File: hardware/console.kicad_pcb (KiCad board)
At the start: 2 copper layers, 44 x 72 mm, 51 parts, among them J1 USB-C_Module, J3 SWD, J4 UART, J5 LiPo_140mAh, SW1 SW_LEFT, SW2 SW_RIGHT, SW3 SW_UP, SW4 SW_DOWN, SW5 SW_A, SW6 SW_B, SW7 SW_POWER, SW8 SW_START, SW9 SW_SELECT, U1 STM32G0B1CBT6, U2 XC6206P332MR, U3 TP4054

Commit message: change the mcu ... again
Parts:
- U1: value STM32G0B1CBT6 -> STM32G070CBT6
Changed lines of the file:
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@@
 			)
 		)
-		(property "Value" "STM32G0B1CBT6"
+		(property "Value" "STM32G070CBT6"
 			(at 0 5.85 0)
 			(layer "F.Fab")
@@
 			)
 		)
-		(property "Datasheet" "https://www.st.com/resource/en/datasheet/stm32g0b1cb.pdf"
+		(property "Datasheet" "https://www.st.com/resource/en/datasheet/stm32g070cb.pdf"
 			(at 0 0 0)
 			(layer "F.Fab")
@@
 			)
 		)
-		(property "Description" "STMicroelectronics Arm Cortex-M0+ MCU, 128KB flash, 144KB RAM, 64 MHz, 1.7-3.6V, USB 2.0 FS, 44 GPIO, LQFP48"
+		(property "Description" "STMicroelectronics Arm Cortex-M0+ MCU, 128KB flash, 36KB RAM, 64 MHz, 2.0-3.6V, 43 GPIO, LQFP48"
 			(at 0 0 0)
 			(layer "F.Fab")
@@
 			)
 		)
-		(property "LCSC" "C2847904"
+		(property "LCSC" "C529338"
 			(at 0 0 0)
 			(unlocked yes)
@@
 			)
 		)
-		(property "MPN" "STM32G0B1CBT6"
+		(property "MPN" "STM32G070CBT6"
 			(at 0 0 0)
 			(unlocked yes)
@@
 			(unit
 				(name "A")
-				(pins "5" "8" "9" "10" "38" "39" "40" "41" "30" "31" "1" "2" "3" "4"
-					"7" "6" "11" "12" "13" "14" "15" "16" "17" "18" "28" "33" "29" "34"
-					"32" "35" "36" "37" "19" "20" "21" "42" "43" "44" "45" "46" "47" "48"
-					"22" "23" "24" "25" "26" "27"
+				(pins "10" "5" "8" "9" "38" "39" "40" "41" "30" "31" "1" "2" "3" "32"
+					"29" "4" "7" "6" "11" "12" "13" "14" "15" "16" "17" "18" "28" "33" "34"
+					"35" "36" "37" "19" "20" "21" "42" "43" "44" "45" "46" "47" "48" "22"
+					"23" "24" "25" "26" "27"
 				)
 			)
@@
 			(roundrect_rratio 0.25)
 			(net "/NRST")
-			(pinfunction "PF2_10")
-			(pintype "bidirectional")
+			(pinfunction "NRST_10")
+			(pintype "input")
 		)
 		(pad "11" smd roundrect
@@
 			(layers "F.Cu" "F.Mask" "F.Paste")
 			(roundrect_rratio 0.25)
-			(net "unconnected-(U1-PA9{slash}UCPD1_DBCC1-Pad29)")
-			(pinfunction "PA9/UCPD1_DBCC1_29")
-			(pintype "bidirectional+no_connect")
+			(net "unconnected-(U1-NC{slash}PA9-Pad29)")
+			(pinfunction "NC/PA9_29")
+			(pintype "no_connect")
 		)
 		(pad "30" smd roundrect
@@
 			(layers "F.Cu" "F.Mask" "F.Paste")
 			(roundrect_rratio 0.25)
-			(net "unconnected-(U1-PA10{slash}UCPD1_DBCC2-Pad32)")
-			(pinfunction "PA10/UCPD1_DBCC2_32")
-			(pintype "bidirectional+no_connect")
+			(net "unconnected-(U1-NC{slash}PA10-Pad32)")
+			(pinfunction "NC/PA10_32")
+			(pintype "no_connect")
 		)
 		(pad "33" smd roundrect

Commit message: pushbutton values
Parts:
- SW1: value SW_LEFT -> SW_PUSH
- SW2: value SW_RIGHT -> SW_PUSH
- SW3: value SW_UP -> SW_PUSH
- SW4: value SW_DOWN -> SW_PUSH
- SW5: value SW_A -> SW_PUSH
- SW6: value SW_B -> SW_PUSH
- SW8: value SW_START -> SW_PUSH
- SW9: value SW_SELECT -> SW_PUSH
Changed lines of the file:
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@@
 			)
 		)
-		(property "Value" "SW_RIGHT"
+		(property "Value" "SW_PUSH"
 			(at 0 2.65 90)
 			(layer "F.Fab")
@@
 			)
 		)
-		(property "Value" "SW_START"
+		(property "Value" "SW_PUSH"
 			(at 0.000001 2.65 335)
 			(layer "F.Fab")
@@
 			)
 		)
-		(property "Value" "SW_UP"
+		(property "Value" "SW_PUSH"
 			(at 0 2.65 0)
 			(layer "F.Fab")
@@
 			)
 		)
-		(property "Value" "SW_A"
+		(property "Value" "SW_PUSH"
 			(at 0 2.65 0)
 			(layer "F.Fab")
@@
 			)
 		)
-		(property "Value" "SW_DOWN"
+		(property "Value" "SW_PUSH"
 			(at 0 2.65 0)
 			(layer "F.Fab")
@@
 			)
 		)
-		(property "Value" "SW_B"
+		(property "Value" "SW_PUSH"
 			(at 0 2.65 0)
 			(layer "F.Fab")
@@
 			)
 		)
-		(property "Value" "SW_SELECT"
+		(property "Value" "SW_PUSH"
 			(at 0.000001 2.65 335)
 			(layer "F.Fab")
@@
 			)
 		)
-		(property "Value" "SW_LEFT"
+		(property "Value" "SW_PUSH"
 			(at 0 2.65 90)
 			(layer "F.Fab")

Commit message: delete more stuff
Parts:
- removed TP3: +3.3V, TestPoint:TestPoint_THTPad_D1.5mm_Drill0.7mm
- removed TP4: VBUS, TestPoint:TestPoint_THTPad_D1.5mm_Drill0.7mm
- removed TP8: I2C_SDA, TestPoint:TestPoint_THTPad_D1.5mm_Drill0.7mm
- removed TP9: I2C_SCL, TestPoint:TestPoint_THTPad_D1.5mm_Drill0.7mm
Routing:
- net /I2C_SDA: track 46.2 -> 44.1 mm
- net VBUS: vias 0 -> 1
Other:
- board text removed: "3V3"
- board text removed: "SCL"
- board text removed: "SDA"
- board text removed: "VB"

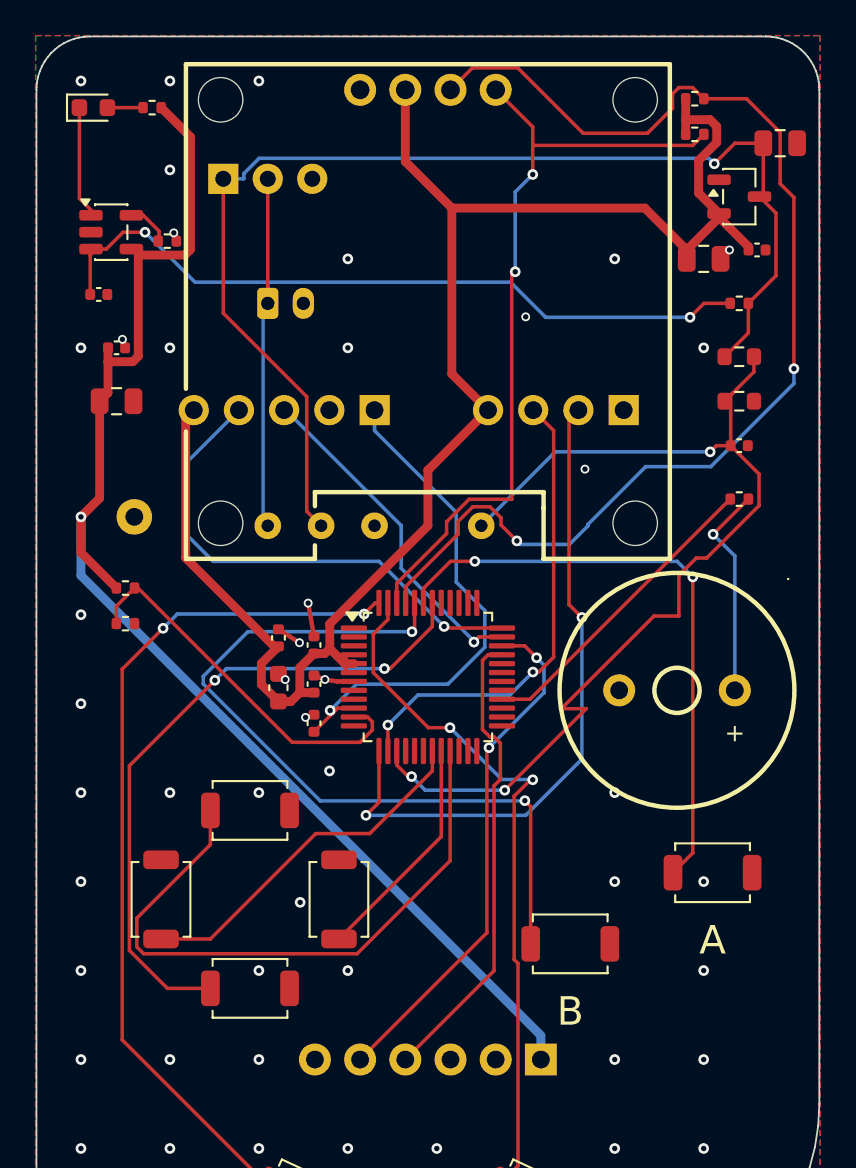
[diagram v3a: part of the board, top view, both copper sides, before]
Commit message: move switch and chrg led to the top right
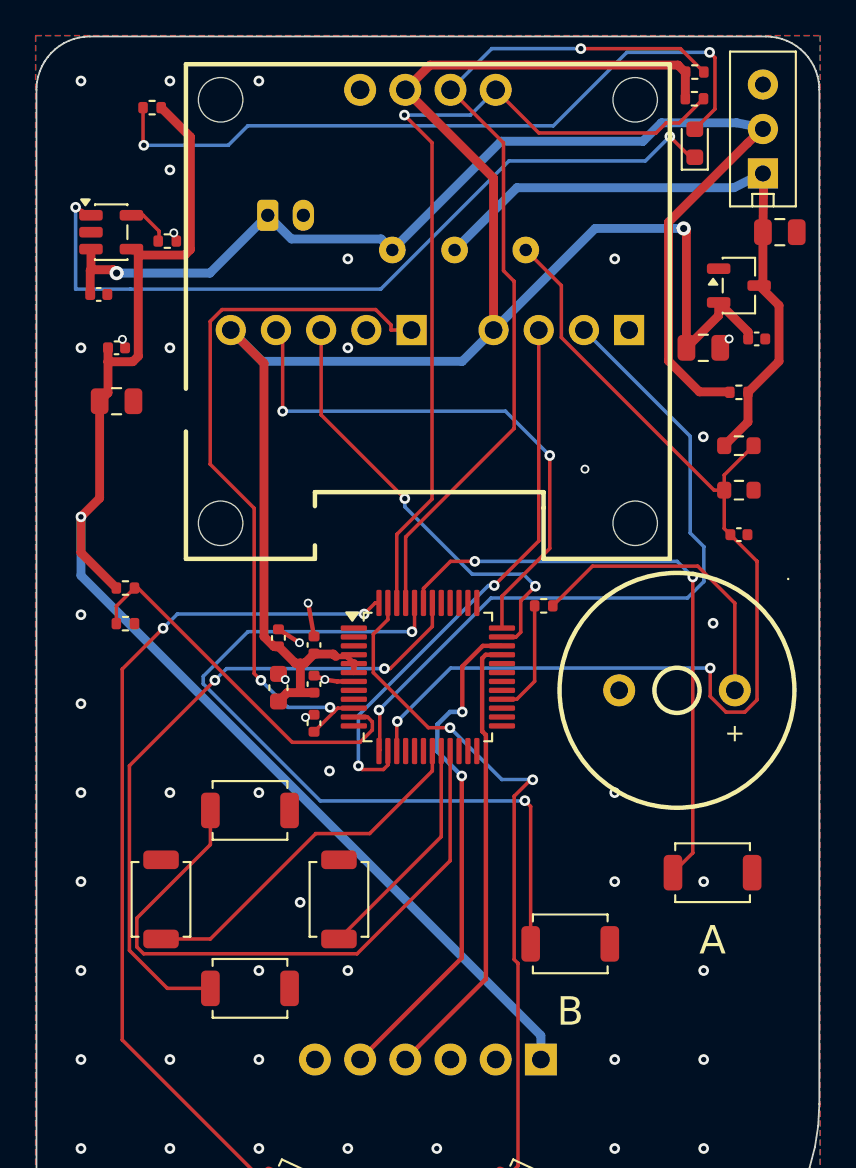
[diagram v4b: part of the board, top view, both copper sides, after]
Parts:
- removed TP1: GND, TestPoint:TestPoint_Loop_D2.50mm_Drill1.0mm
- removed TP2: GND, TestPoint:TestPoint_THTPad_D1.5mm_Drill0.7mm
- SW7: moved to F.Cu
- moved D1 33.9 mm to (37.0, 6.00), turned to 90 degrees
- moved SW7 28.0 mm to (40.8, 5.20), turned to 90 degrees
- moved TP6 17.2 mm to (23.5, 12.0)
- moved TP5 17.0 mm to (20.0, 12.0)
- moved TP7 15.7 mm to (27.5, 12.0)
- moved R6 12.5 mm to (28.5, 32.0)
- moved C12 5.00 mm to (39.5, 28.0)
- moved C2 5.00 mm to (37.5, 17.5)
- moved C3 5.00 mm to (41.8, 11.0)
- moved C4 5.00 mm to (40.5, 17.0)
- moved R1 5.00 mm to (39.5, 20.0)
- moved R10 5.00 mm to (39.5, 25.5)
- moved R9 5.00 mm to (39.5, 23.0)
- moved U2 5.00 mm to (39.5, 14.0)
- moved J3 4.96 mm to (21.1, 16.5)
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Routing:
- net Net-(D1-A): track 2.00 -> 41.0 mm, vias 0 -> 2
- net /CHG_LED: track 6.44 -> 44.4 mm, vias 0 -> 2
- net /VBAT_SW: track 67.0 -> 36.2 mm, vias 1 -> 0
- net /I2C_SCL: track 67.5 -> 48.6 mm, vias 2 -> 1
- net /NRST: track 29.1 -> 41.2 mm, vias 1 -> 2
- net /SPK_PWM: track 17.5 -> 6.50 mm
- net +3.3V: track 94.2 -> 104.1 mm, vias 0 -> 1
- net /SWDIO: track 19.2 -> 25.2 mm, vias 1 -> 2
- net Net-(LS1-+): track 12.1 -> 16.9 mm, vias 1 -> 0
- net /UART_RX: track 26.7 -> 31.5 mm
- net /I2C_SDA: track 44.1 -> 48.1 mm, vias 2 -> 1
- net /SWCLK: track 28.1 -> 31.6 mm, vias 1 -> 2
- net /VBAT_LIPO: track 61.9 -> 65.1 mm, vias 2 -> 1
- net /UART_TX: track 37.5 -> 40.5 mm, vias 2 -> 1
- net /VBAT_SENSE: track 58.6 -> 59.6 mm, vias 3 -> 2
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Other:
- board text added: "3V"
- board text added: "CLK"
- board text added: "DIO"
- board text added: "GND"
- board text added: "NRST"
- board text added: "RX"
- board text added: "TX"
- board text removed: "G"
- board text removed: "PWR"
- board text removed: "UART"

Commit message: more silkscreen
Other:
- board text added: "Board Rev 1.0"
- board text added: "JLCJLCJLCJLC"
- board text added: "LiPo Battery 140mAh"
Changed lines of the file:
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@@
 		)
 	)
+	(gr_rect
+		(start 8 29.5)
+		(end 28 54.5)
+		(stroke
+			(width 0.25)
+			(type default)
+		)
+		(fill no)
+		(layer "B.SilkS")
+	)
 	(gr_line
 		(start 0 3)
@@
 		)
 	)
+	(gr_text "JLCJLCJLCJLC"
+		(at 36 53.5 0)
+		(layer "B.SilkS")
+		(effects
+			(font
+				(size 1 0.8)
+				(thickness 0.15)
+			)
+			(justify mirror)
+		)
+	)
 	(gr_text "3V"
 		(at 11 19.7 90)
@@
 		)
 	)
+	(gr_text "Board Rev 1.0"
+		(at 41.5 51.5 0)
+		(layer "B.SilkS")
+		(effects
+			(font
+				(size 1 1)
+				(thickness 0.1)
+			)
+			(justify left bottom mirror)
+		)
+	)
 	(gr_text "SWD"
 		(at 5.5 21 0)
@@
 		)
 	)
+	(gr_text "LiPo Battery\n  140mAh"
+		(at 23.5 44 0)
+		(layer "B.SilkS")
+		(effects
+			(font
+				(size 1 1)
+				(thickness 0.2)
+				(bold yes)
+			)
+			(justify left bottom mirror)
+		)
+	)
 	(gr_text "USB-C"
-		(at 22 54.4 0)
+		(at 21 62.5 0)
 		(layer "B.SilkS")
 		(effects
@@
 		)
 	)
+	(group ""
+		(members "8b05adc4-59e0-418b-bc93-a64cdb273640" "a4d435df-7e56-4c38-b6c9-03b8eea75950")
+	)
 	(embedded_fonts no)

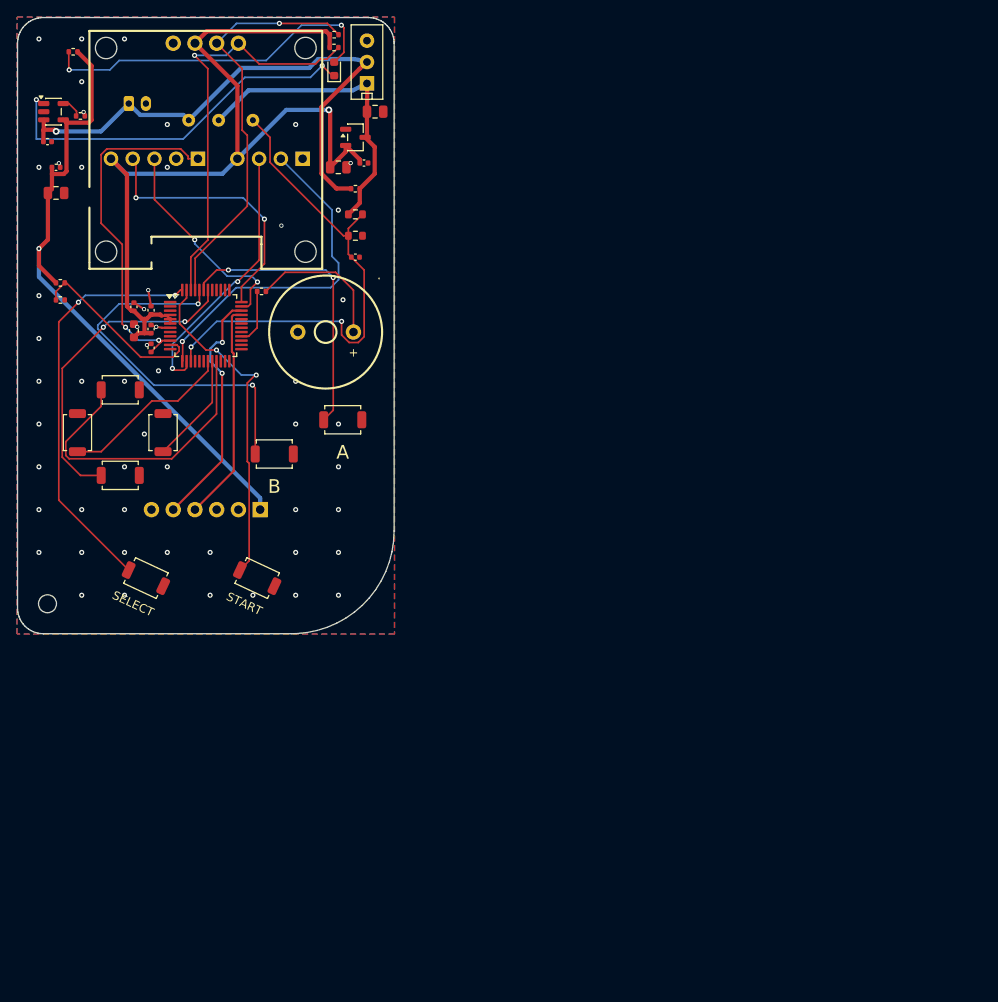
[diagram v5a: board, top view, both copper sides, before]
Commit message: fix battery connector
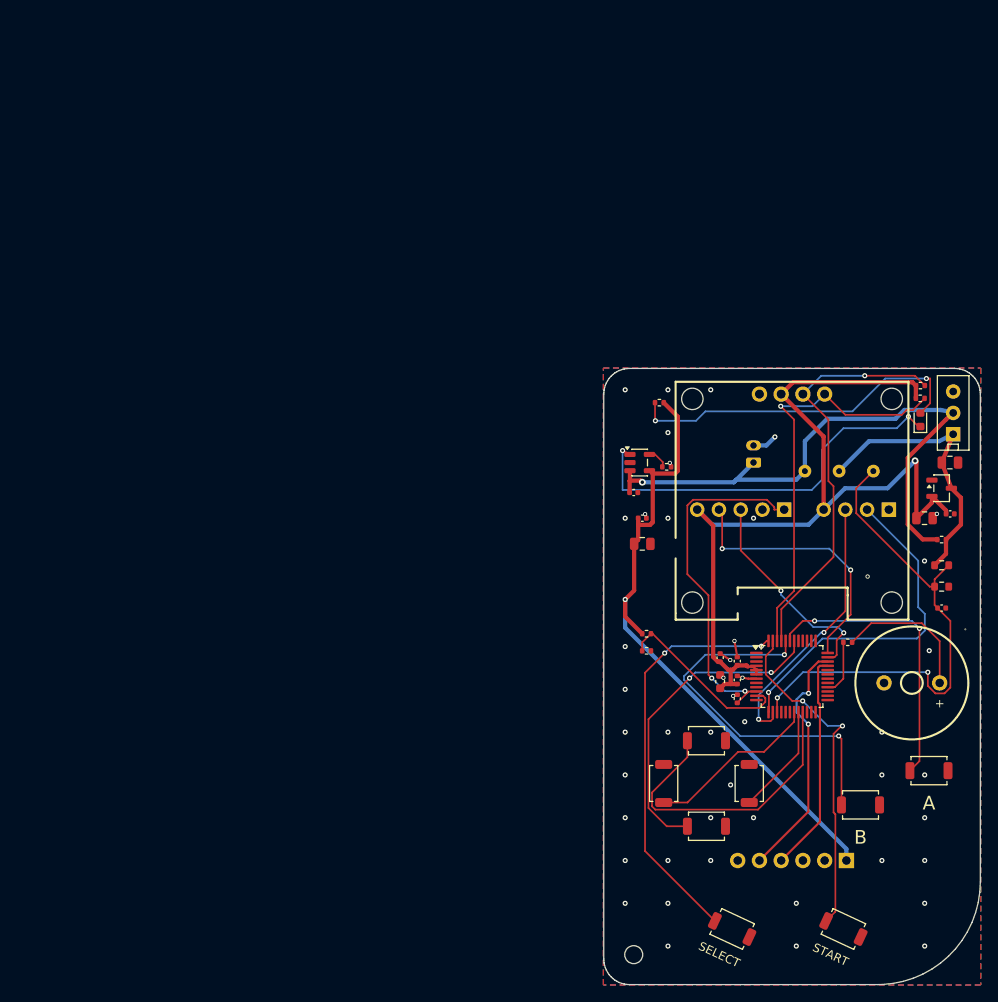
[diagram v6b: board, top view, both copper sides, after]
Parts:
- J5: footprint Connector_JST:JST_PH_B2B-PH-K_1x02_P2.00mm_Vertical -> Connector_JST:JST_PH_S2B-PH-K_1x02_P2.00mm_Horizontal
- moved J5 84.2 mm to (86.0, 52.0), turned to 90 degrees
- moved TP6 83.3 mm to (96.0, 53.0)
- moved TP7 83.3 mm to (100.0, 53.0)
- moved TP5 82.9 mm to (92.0, 53.0)
- moved C1 79.8 mm to (73.0, 58.5)
- moved C10 79.8 mm to (73.0, 61.5)
- moved C11 79.8 mm to (72.0, 55.5)
- moved C12 79.8 mm to (108.0, 69.0)
- moved C2 79.8 mm to (106.0, 58.5)
- moved C4 79.8 mm to (109.0, 58.0)
- moved C5 79.8 mm to (82.1, 77.6)
- moved C6 79.8 mm to (84.1, 77.4)
- moved C7 79.8 mm to (82.1, 74.8)
- moved C8 79.8 mm to (84.1, 75.2)
- moved C9 79.8 mm to (84.1, 79.6)
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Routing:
- net /VBAT_LIPO: track 65.1 -> 68.8 mm
- net /VBAT_SW: track 36.2 -> 32.5 mm
- net GND: track 8.08 -> 11.0 mm, vias 53 -> 46
- net /CHG_LED: track 44.4 -> 46.5 mm

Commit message: change buzzer
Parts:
- added TH1: ToolingHole, console:TOOL-NPTH-D1.152, F.Cu at (71.2, 47.0)
- added TH2: ToolingHole, console:TOOL-NPTH-D1.152, F.Cu at (108.2, 106.0)
- LS1: value HNR-1207PA6.5 -> PS1240P02BT; footprint console:BUZ-TH_BD12.5-P6.50-D0.9 -> Buzzer_Beeper:Buzzer_TDK_PS1240P02BT_D12.2mm_H6.5mm
- moved LS1 2.50 mm to (107.0, 77.8)
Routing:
- net /VBAT_SENSE: track 59.6 -> 55.5 mm
